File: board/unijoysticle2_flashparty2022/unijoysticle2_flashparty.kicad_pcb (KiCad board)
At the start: 2 copper layers, 61 x 55.2 mm, 20 parts, among them J1 DB9_Female, J2 DB9_Female, SW1 SW_Push, U1 74HC05, U2 74HC05, U3 mini_esp32

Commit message: Unijoysticle2 Flashparty edition rev A
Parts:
- removed D4: 1N5819, Diode_THT:D_DO-41_SOD81_P7.62mm_Horizontal
- added D3: 1N5819, Diode_THT:D_DO-41_SOD81_P7.62mm_Horizontal, F.Cu at (142.7, 92.2)
- added G***: LOGO, bmp:fp, F.Cu at (194.3, 124.5)
- added G***: LOGO, bmp:flashparty, B.Cu at (142.5, 100.3)
- moved R5 6.60 mm to (169.9, 117.9), turned to 180 degrees
- moved R6 4.88 mm to (169.9, 120.7), turned to 180 degrees
- moved C2 0.34 mm to (148.1, 86.0)
- moved C1 0.09 mm to (114.6, 86.0)
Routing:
- net GPIO_BOOTSTRAP_04: track 13.6 -> 4.32 mm
- net GPIO_BOOTSTRAP_15_LED_BT: track 15.0 -> 9.14 mm
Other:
- rule pad_to_mask_clearance: 0.0508 -> 0
- board text added: "L.I.A."
- board text added: "Unijoysticle 2"
- board text added: "edition"
- board text removed: "Rev F"
- board text removed: "Unijoysticle 2 http://retro.moe"

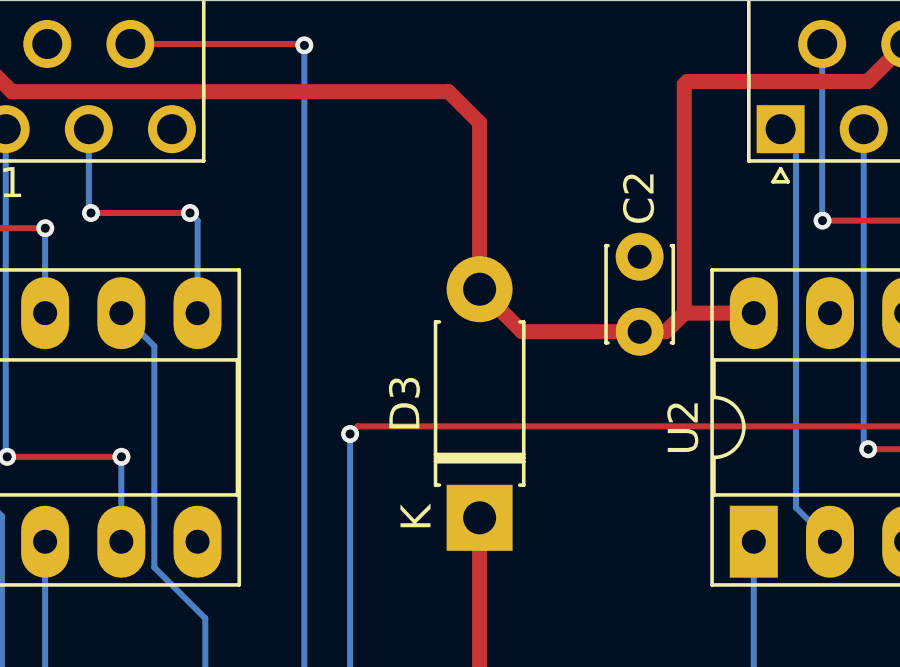
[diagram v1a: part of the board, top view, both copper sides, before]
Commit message: flashparty / c64: remove warnings introduced in kicad 6.0.10
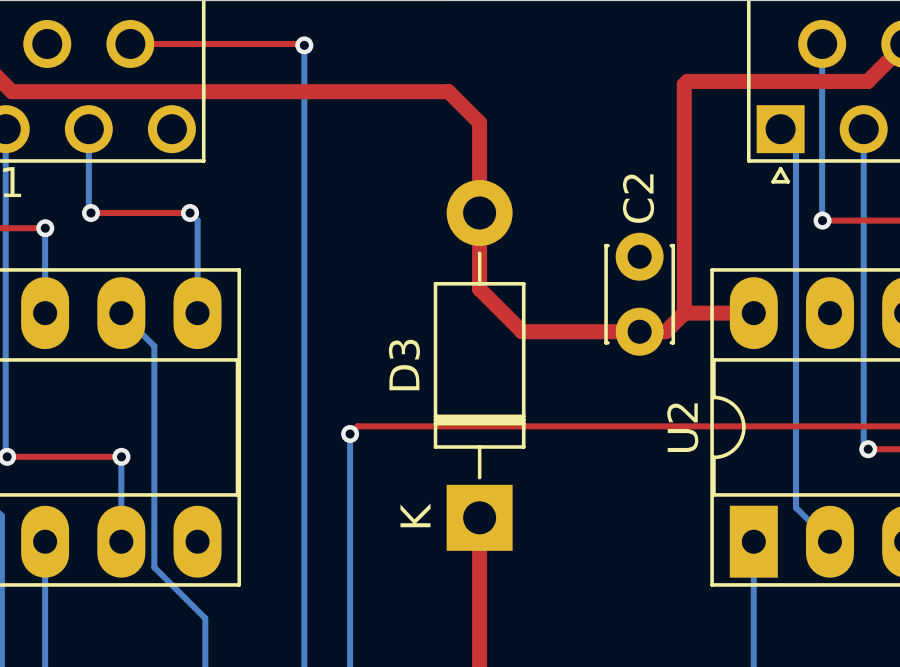
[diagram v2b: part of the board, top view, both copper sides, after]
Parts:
- D3: footprint Diode_THT:D_DO-41_SOD81_P7.62mm_Horizontal -> Diode_THT:D_DO-41_SOD81_P10.16mm_Horizontal
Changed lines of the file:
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@@
     )
   )
-  (footprint "Diode_THT:D_DO-41_SOD81_P7.62mm_Horizontal" (layer "F.Cu")
+  (footprint "Diode_THT:D_DO-41_SOD81_P10.16mm_Horizontal" (layer "F.Cu")
     (at 142.748 92.202 90)
-    (descr "Diode, DO-41_SOD81 series, Axial, Horizontal, pin pitch=7.62mm, , length*diameter=5.2*2.7mm^2, , http://www.diodes.com/_files/packages/DO-41%20(Plastic).pdf")
-    (tags "Diode DO-41_SOD81 series Axial Horizontal pin pitch 7.62mm  length 5.2mm diameter 2.7mm")
+    (descr "Diode, DO-41_SOD81 series, Axial, Horizontal, pin pitch=10.16mm, , length*diameter=5.2*2.7mm^2, , http://www.diodes.com/_files/packages/DO-41%20(Plastic).pdf")
+    (tags "Diode DO-41_SOD81 series Axial Horizontal pin pitch 10.16mm  length 5.2mm diameter 2.7mm")
     (property "Sheetfile" "unijoysticle2_flashparty.kicad_sch")
     (property "Sheetname" "")
     (attr through_hole)
-    (fp_text reference "D3" (at 3.81 -2.47 90) (layer "F.SilkS")
+    (fp_text reference "D3" (at 5.08 -2.47 90) (layer "F.SilkS")
       (effects (font (size 1 1) (thickness 0.15)))
     )
-    (fp_text value "1N5819" (at 3.81 2.47 90) (layer "F.Fab")
+    (fp_text value "1N5819" (at 5.08 2.47 90) (layer "F.Fab")
       (effects (font (size 1 1) (thickness 0.15)))
     )
@@
       (effects (font (size 1 1) (thickness 0.15)))
     )
-    (fp_text user "${REFERENCE}" (at 4.2 0 90) (layer "F.Fab")
+    (fp_text user "${REFERENCE}" (at 5.47 0 90) (layer "F.Fab")
       (effects (font (size 1 1) (thickness 0.15)))
     )
-    (fp_line (start 1.99 -1.47) (end 1.99 1.47) (layer "F.SilkS") (width 0.12))
-    (fp_line (start 6.53 -1.47) (end 6.53 -1.34) (layer "F.SilkS") (width 0.12))
-    (fp_line (start 1.09 -1.47) (end 6.53 -1.47) (layer "F.SilkS") (width 0.12))
-    (fp_line (start 1.09 1.34) (end 1.09 1.47) (layer "F.SilkS") (width 0.12))
-    (fp_line (start 1.09 -1.34) (end 1.09 -1.47) (layer "F.SilkS") (width 0.12))
-    (fp_line (start 2.11 -1.47) (end 2.11 1.47) (layer "F.SilkS") (width 0.12))
-    (fp_line (start 1.87 -1.47) (end 1.87 1.47) (layer "F.SilkS") (width 0.12))
-    (fp_line (start 1.09 1.47) (end 6.53 1.47) (layer "F.SilkS") (width 0.12))
-    (fp_line (start 6.53 1.47) (end 6.53 1.34) (layer "F.SilkS") (width 0.12))
-    (fp_line (start 8.97 1.6) (end 8.97 -1.6) (layer "F.CrtYd") (width 0.05))
-    (fp_line (start 8.97 -1.6) (end -1.35 -1.6) (layer "F.CrtYd") (width 0.05))
-    (fp_line (start -1.35 1.6) (end 8.97 1.6) (layer "F.CrtYd") (width 0.05))
+    (fp_line (start 3.14 -1.47) (end 3.14 1.47) (layer "F.SilkS") (width 0.12))
+    (fp_line (start 3.38 -1.47) (end 3.38 1.47) (layer "F.SilkS") (width 0.12))
+    (fp_line (start 7.8 -1.47) (end 2.36 -1.47) (layer "F.SilkS") (width 0.12))
+    (fp_line (start 3.26 -1.47) (end 3.26 1.47) (layer "F.SilkS") (width 0.12))
+    (fp_line (start 7.8 1.47) (end 7.8 -1.47) (layer "F.SilkS") (width 0.12))
+    (fp_line (start 2.36 -1.47) (end 2.36 1.47) (layer "F.SilkS") (width 0.12))
+    (fp_line (start 8.82 0) (end 7.8 0) (layer "F.SilkS") (width 0.12))
+    (fp_line (start 1.34 0) (end 2.36 0) (layer "F.SilkS") (width 0.12))
+    (fp_line (start 2.36 1.47) (end 7.8 1.47) (layer "F.SilkS") (width 0.12))
+    (fp_line (start -1.35 1.6) (end 11.51 1.6) (layer "F.CrtYd") (width 0.05))
     (fp_line (start -1.35 -1.6) (end -1.35 1.6) (layer "F.CrtYd") (width 0.05))
-    (fp_line (start 1.21 -1.35) (end 1.21 1.35) (layer "F.Fab") (width 0.1))
-    (fp_line (start 7.62 0) (end 6.41 0) (layer "F.Fab") (width 0.1))
-    (fp_line (start 1.99 -1.35) (end 1.99 1.35) (layer "F.Fab") (width 0.1))
-    (fp_line (start 6.41 -1.35) (end 1.21 -1.35) (layer "F.Fab") (width 0.1))
-    (fp_line (start 0 0) (end 1.21 0) (layer "F.Fab") (width 0.1))
-    (fp_line (start 6.41 1.35) (end 6.41 -1.35) (layer "F.Fab") (width 0.1))
-    (fp_line (start 1.89 -1.35) (end 1.89 1.35) (layer "F.Fab") (width 0.1))
-    (fp_line (start 1.21 1.35) (end 6.41 1.35) (layer "F.Fab") (width 0.1))
-    (fp_line (start 2.09 -1.35) (end 2.09 1.35) (layer "F.Fab") (width 0.1))
+    (fp_line (start 11.51 1.6) (end 11.51 -1.6) (layer "F.CrtYd") (width 0.05))
+    (fp_line (start 11.51 -1.6) (end -1.35 -1.6) (layer "F.CrtYd") (width 0.05))
+    (fp_line (start 10.16 0) (end 7.68 0) (layer "F.Fab") (width 0.1))
+    (fp_line (start 3.26 -1.35) (end 3.26 1.35) (layer "F.Fab") (width 0.1))
+    (fp_line (start 2.48 -1.35) (end 2.48 1.35) (layer "F.Fab") (width 0.1))
+    (fp_line (start 0 0) (end 2.48 0) (layer "F.Fab") (width 0.1))
+    (fp_line (start 3.36 -1.35) (end 3.36 1.35) (layer "F.Fab") (width 0.1))
+    (fp_line (start 3.16 -1.35) (end 3.16 1.35) (layer "F.Fab") (width 0.1))
+    (fp_line (start 7.68 -1.35) (end 2.48 -1.35) (layer "F.Fab") (width 0.1))
+    (fp_line (start 2.48 1.35) (end 7.68 1.35) (layer "F.Fab") (width 0.1))
+    (fp_line (start 7.68 1.35) (end 7.68 -1.35) (layer "F.Fab") (width 0.1))
     (pad "1" thru_hole rect (at 0 0 90) (size 2.2 2.2) (drill 1.1) (layers *.Cu *.Mask)
       (net 24 "VDD") (pinfunction "K") (pintype "passive"))
-    (pad "2" thru_hole oval (at 7.62 0 90) (size 2.2 2.2) (drill 1.1) (layers *.Cu *.Mask)
+    (pad "2" thru_hole oval (at 10.16 0 90) (size 2.2 2.2) (drill 1.1) (layers *.Cu *.Mask)
       (net 29 "+5V") (pinfunction "A") (pintype "passive"))
-    (model "${KICAD6_3DMODEL_DIR}/Diode_THT.3dshapes/D_DO-41_SOD81_P7.62mm_Horizontal.wrl"
+    (model "${KICAD6_3DMODEL_DIR}/Diode_THT.3dshapes/D_DO-41_SOD81_P10.16mm_Horizontal.wrl"
       (offset (xyz 0 0 0))
       (scale (xyz 1 1 1))
